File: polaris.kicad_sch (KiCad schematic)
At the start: 21 parts, among them J101 XT60-M, J102 SPI, J103 PYRO5, J104 I2C, J105 PYRO4, J106 PYRO3, J107 PB, J108 PYRO2, J109 PYRO1, J110 SWD, J111 PYRO0, J112 SERVO0, J113 SERVO1, J114 SERVO2, J115 SERVO3, J116 SERVO4, J117 SERVO5

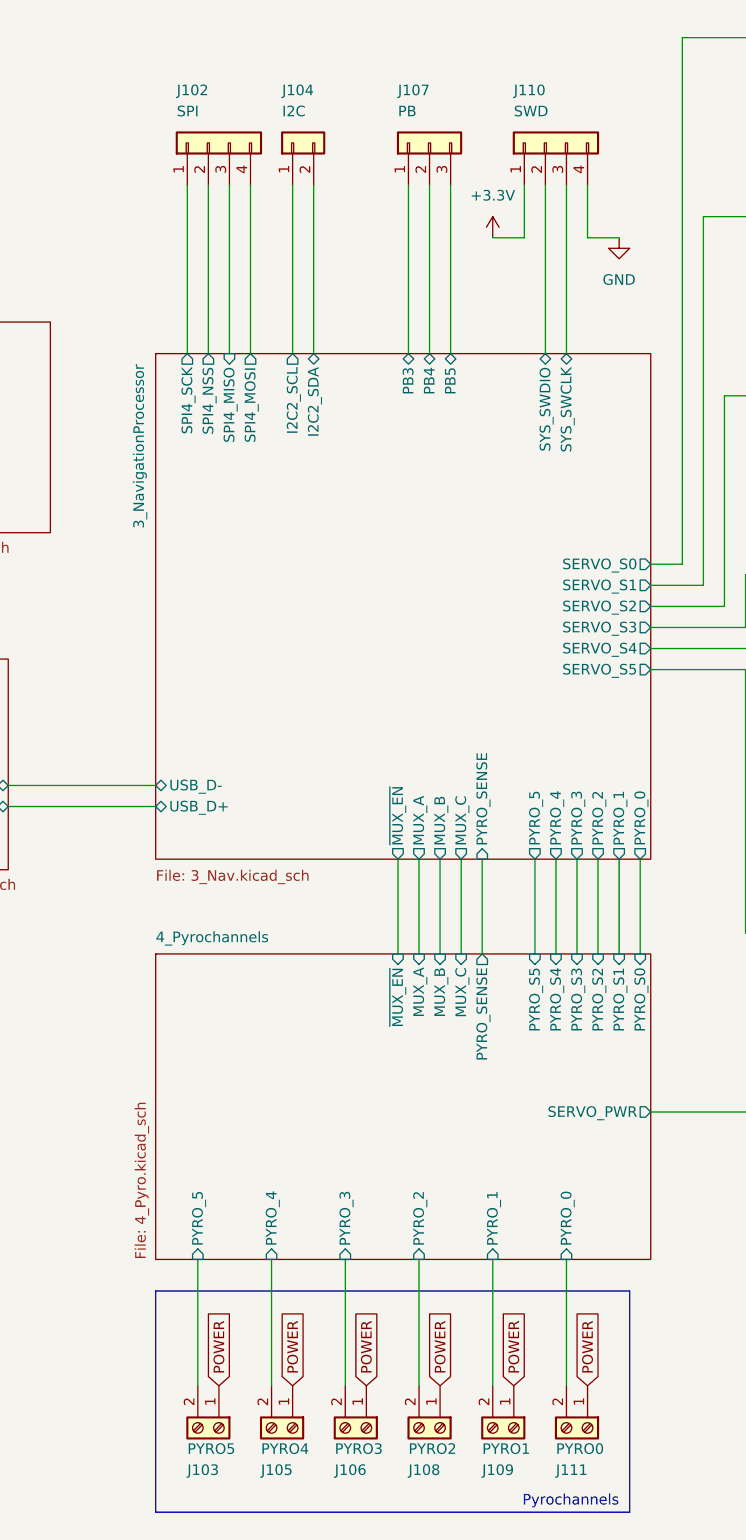
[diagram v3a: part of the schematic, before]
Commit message: Continued laying traces
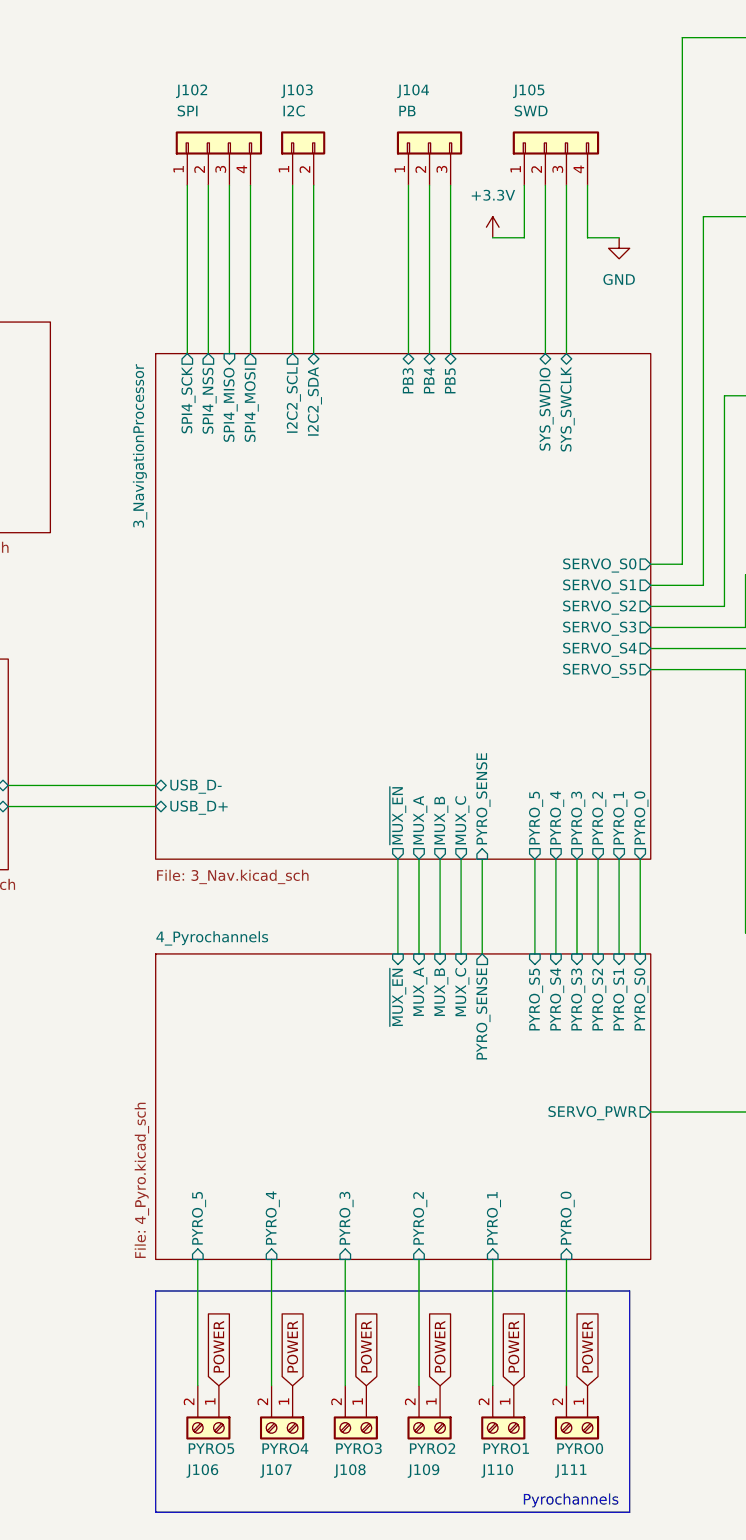
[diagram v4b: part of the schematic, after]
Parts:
- renumbered J104 to J103, J107 to J104, J110 to J105, J103 to J106, J105 to J107, J106 to J108, J108 to J109, J109 to J110
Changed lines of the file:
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@@
 		(in_pos_files yes)
 		(dnp no)
-		(property "Reference" "J107"
+		(property "Reference" "J104"
 			(at 139.7 22.86 90)
 			(show_name no)
@@
 			(project "polaris"
 				(path "/cfb90e19-9fbe-47a1-a5ac-df522853d1d0"
-					(reference "J107")
+					(reference "J104")
 					(unit 1)
 				)
@@
 		(in_pos_files yes)
 		(dnp no)
-		(property "Reference" "J103"
+		(property "Reference" "J106"
 			(at 114.3 189.23 90)
 			(show_name no)
@@
 			(project "polaris"
 				(path "/cfb90e19-9fbe-47a1-a5ac-df522853d1d0"
-					(reference "J103")
+					(reference "J106")
 					(unit 1)
 				)
@@
 		(in_pos_files yes)
 		(dnp no)
-		(property "Reference" "J110"
+		(property "Reference" "J105"
 			(at 153.67 22.86 90)
 			(show_name no)
@@
 			(project "polaris"
 				(path "/cfb90e19-9fbe-47a1-a5ac-df522853d1d0"
-					(reference "J110")
+					(reference "J105")
 					(unit 1)
 				)
@@
 		(in_pos_files yes)
 		(dnp no)
-		(property "Reference" "J109"
+		(property "Reference" "J110"
 			(at 149.86 189.23 90)
 			(show_name no)
@@
 			(project "polaris"
 				(path "/cfb90e19-9fbe-47a1-a5ac-df522853d1d0"
-					(reference "J109")
+					(reference "J110")
 					(unit 1)
 				)
@@
 		(in_pos_files yes)
 		(dnp no)
-		(property "Reference" "J104"
+		(property "Reference" "J103"
 			(at 125.73 22.86 90)
 			(show_name no)
@@
 			(project "polaris"
 				(path "/cfb90e19-9fbe-47a1-a5ac-df522853d1d0"
-					(reference "J104")
+					(reference "J103")
 					(unit 1)
 				)
@@
 		(in_pos_files yes)
 		(dnp no)
-		(property "Reference" "J105"
+		(property "Reference" "J107"
 			(at 123.19 189.23 90)
 			(show_name no)
@@
 			(project "polaris"
 				(path "/cfb90e19-9fbe-47a1-a5ac-df522853d1d0"
-					(reference "J105")
+					(reference "J107")
 					(unit 1)
 				)
@@
 		(in_pos_files yes)
 		(dnp no)
-		(property "Reference" "J106"
+		(property "Reference" "J108"
 			(at 132.08 189.23 90)
 			(show_name no)
@@
 			(project "polaris"
 				(path "/cfb90e19-9fbe-47a1-a5ac-df522853d1d0"
-					(reference "J106")
+					(reference "J108")
 					(unit 1)
 				)
@@
 		(in_pos_files yes)
 		(dnp no)
-		(property "Reference" "J108"
+		(property "Reference" "J109"
 			(at 140.97 189.23 90)
 			(show_name no)
@@
 			(project "polaris"
 				(path "/cfb90e19-9fbe-47a1-a5ac-df522853d1d0"
-					(reference "J108")
+					(reference "J109")
 					(unit 1)
 				)

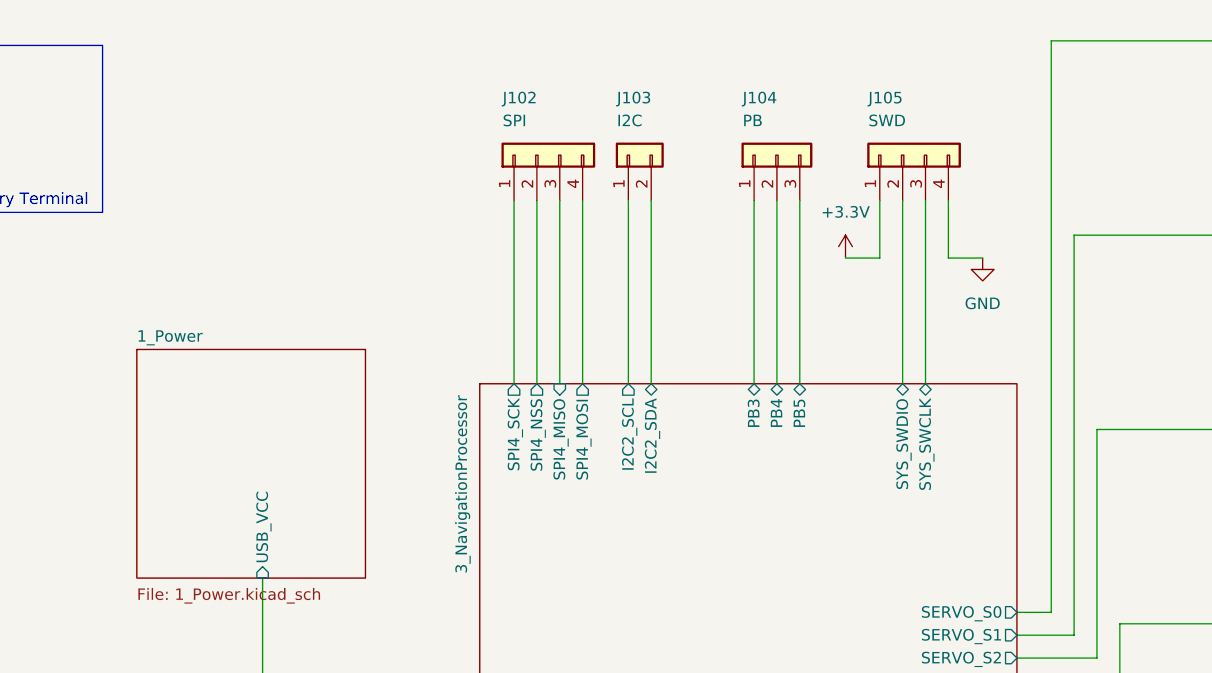
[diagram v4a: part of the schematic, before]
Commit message: Updated board to support any telemetry radio
Continued laying traces
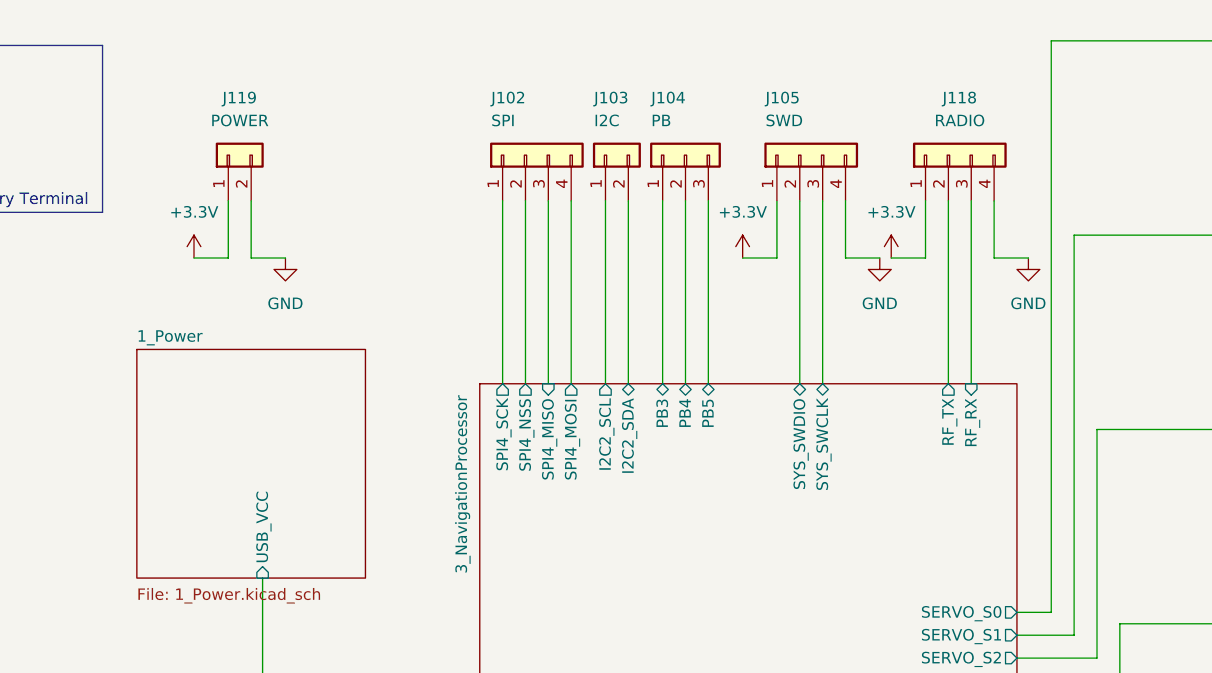
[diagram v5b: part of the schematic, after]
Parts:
- added J118: RADIO, Connector_JST:JST_XH_B4B-XH-A_1x04_P2.50mm_Vertical, symbol Connector_Generic:Conn_01x04
- added J119: POWER, TerminalBlock:TerminalBlock_Xinya_XY308-2.54-2P_1x02_P2.54mm_Horizontal, symbol Connector_Generic:Conn_01x02
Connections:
- net +3.3V: now also J118.1 (Pin_1), J119.1 (Pin_1)
- net GND: now also J118.4 (Pin_4), J119.2 (Pin_2)
- new net 3_NavigationProcessor/RF_RX: J118.3 (Pin_3)
- new net 3_NavigationProcessor/RF_TX: J118.2 (Pin_2)
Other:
- sheet 3_NavigationProcessor ports: added RF_RX, RF_TX; removed none
- moved on the sheet: J102, J103, J104, J105
